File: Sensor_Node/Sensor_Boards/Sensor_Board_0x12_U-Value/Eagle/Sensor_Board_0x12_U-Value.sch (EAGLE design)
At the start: 28 parts, among them IC1 MCP3911A0-E/SS, IC2 4066D, J2 ARDUINO_ISP, J4 1x3 RA Female .1", J5 1x3 RA Female .1", U2 ATMEGA328P_TQFP, Y1 8MHZ

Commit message: Renamed U-value sensor board files
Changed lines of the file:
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@@
 <part name="U$1" library="wsn" deviceset="M04_SMD_90" device=""/>
 <part name="P+6" library="supply1" deviceset="VCC" device=""/>
-<part name="P+7" library="supply1" deviceset="VCC" device=""/>
 <part name="J4" library="wsn" deviceset="M03" device="SMD_RA_FEMALE" value="1x3 RA Female .1&quot;"/>
 <part name="J5" library="wsn" deviceset="M03" device="SMD_RA_FEMALE" value="1x3 RA Female .1&quot;"/>
@@
 <part name="GND17" library="supply1" deviceset="GND" device="" value="DGND"/>
 <part name="GND18" library="supply1" deviceset="GND" device="" value="DGND"/>
-<part name="GND19" library="supply1" deviceset="GND" device="" value="DGND"/>
 <part name="GND20" library="supply1" deviceset="GND" device="" value="DGND"/>
 <part name="GND21" library="supply1" deviceset="GND" device="" value="DGND"/>
@@
 <instance part="U$1" gate="G$1" x="29.21" y="81.788" rot="MR180"/>
 <instance part="P+6" gate="VCC" x="45.01" y="88.42"/>
-<instance part="P+7" gate="VCC" x="142.748" y="85.852"/>
 <instance part="J4" gate="J$1" x="155.194" y="72.898"/>
 <instance part="J5" gate="J$1" x="199.39" y="71.882"/>
@@
 <instance part="GND18" gate="1" x="175.006" y="65.016" smashed="yes">
 <attribute name="VALUE" x="173.736" y="67.556" size="1.778" layer="96" rot="R180"/>
-</instance>
-<instance part="GND19" gate="1" x="128.778" y="67.056" smashed="yes">
-<attribute name="VALUE" x="127.508" y="69.596" size="1.778" layer="96" rot="R180"/>
 </instance>
 <instance part="GND20" gate="1" x="99.568" y="75.692" smashed="yes">
@@
 </segment>
 <segment>
-<wire x1="126.492" y1="78.232" x2="142.748" y2="78.232" width="0.1524" layer="91"/>
-<pinref part="P+7" gate="VCC" pin="VCC"/>
-<wire x1="142.748" y1="78.232" x2="142.748" y2="83.312" width="0.1524" layer="91"/>
-</segment>
-<segment>
 <pinref part="P+6" gate="VCC" pin="VCC"/>
 <pinref part="U$1" gate="G$1" pin="1"/>
@@
 <label x="84.582" y="77.978" size="1.27" layer="95" xref="yes"/>
 </segment>
-<segment>
-<wire x1="126.29" y1="85.88" x2="127.508" y2="85.852" width="0.1524" layer="91"/>
-<label x="127.508" y="85.852" size="1.27" layer="95" xref="yes"/>
-</segment>
 </net>
 <net name="N$3" class="0">
@@
 <net name="FTDI_RXI" class="0">
 <segment>
-<wire x1="126.29" y1="83.34" x2="127.508" y2="83.312" width="0.1524" layer="91"/>
-<label x="127.508" y="83.312" size="1.27" layer="95" xref="yes"/>
-</segment>
-<segment>
 <pinref part="U2" gate="U$1" pin="PD1(TXD)"/>
 <wire x1="246.84" y1="150.65" x2="244.3" y2="150.65" width="0.1524" layer="91"/>
@@
 </net>
 <net name="FTDI_TXO" class="0">
-<segment>
-<wire x1="126.29" y1="80.8" x2="127.508" y2="80.772" width="0.1524" layer="91"/>
-<label x="127.508" y="80.772" size="1.27" layer="95" xref="yes"/>
-</segment>
 <segment>
 <pinref part="U2" gate="U$1" pin="PD0(RXD)"/>
@@
 </segment>
 <segment>
-<wire x1="126.29" y1="73.18" x2="128.778" y2="73.152" width="0.1524" layer="91"/>
-<wire x1="128.778" y1="73.152" x2="128.778" y2="69.596" width="0.1524" layer="91"/>
-<wire x1="126.29" y1="75.72" x2="128.778" y2="75.692" width="0.1524" layer="91"/>
-<wire x1="128.778" y1="75.692" x2="128.778" y2="73.152" width="0.1524" layer="91"/>
-<junction x="128.778" y="73.152"/>
-<pinref part="GND19" gate="1" pin="GND"/>
-</segment>
-<segment>

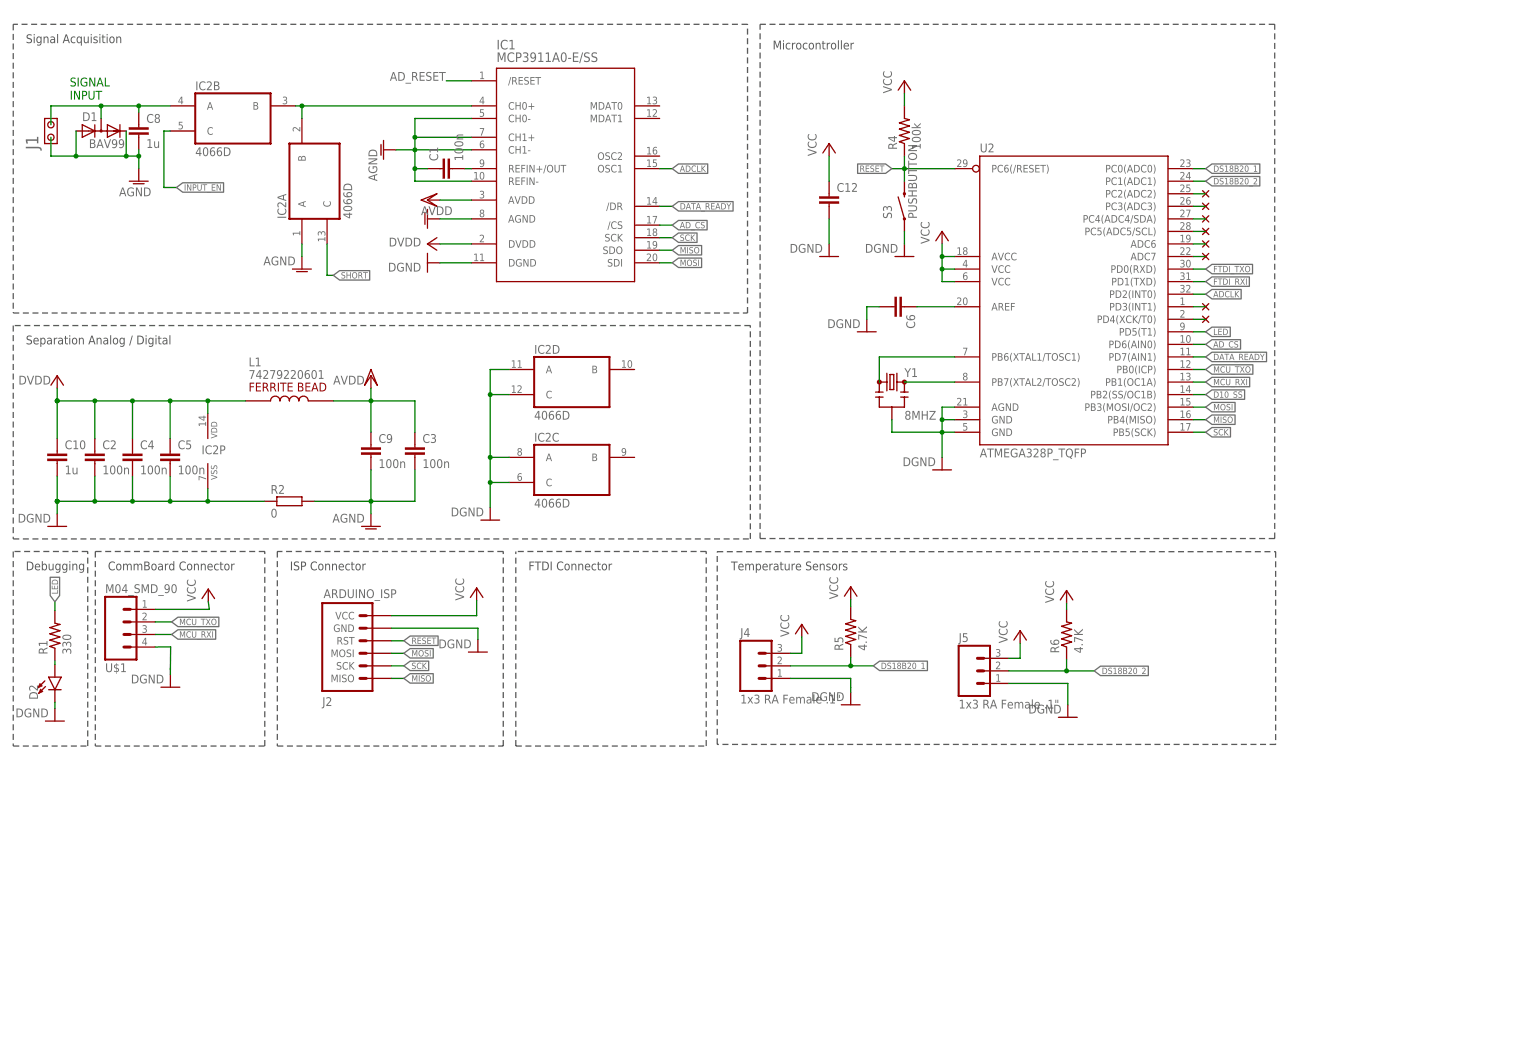
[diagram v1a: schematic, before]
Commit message: Renamed Heat_Flux to U-Value
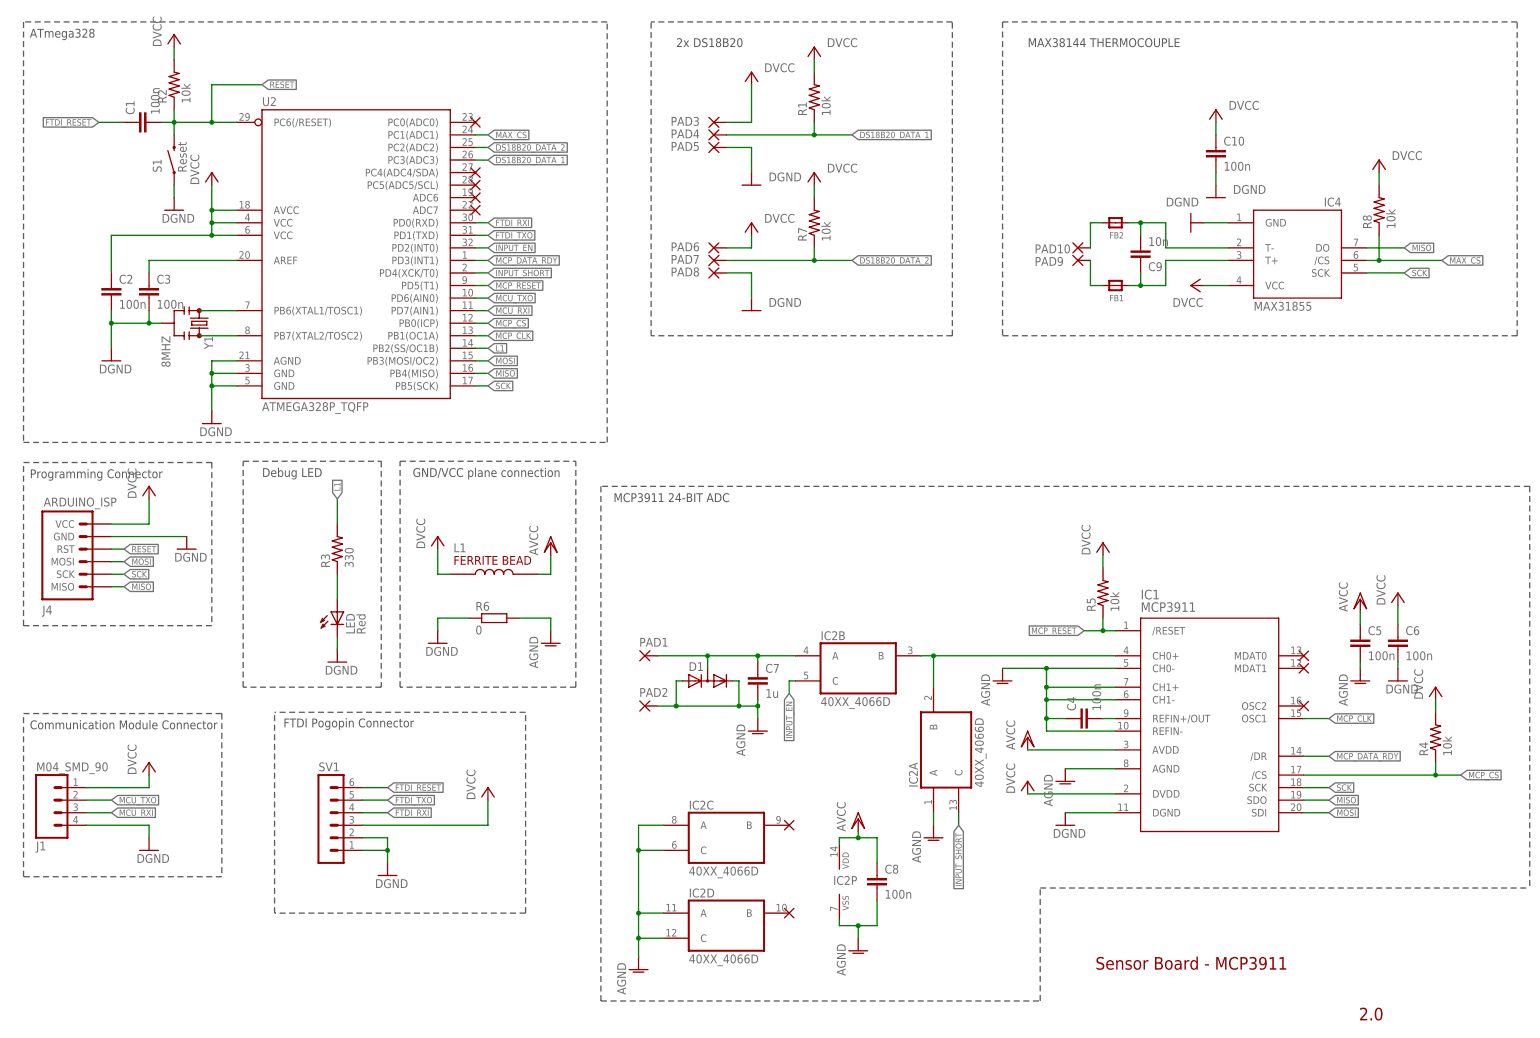
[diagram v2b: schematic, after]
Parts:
- removed C12: (no value), wsn:CAP0805
- removed D2: (no value), wsn:LED0603
- removed J2: ARDUINO_ISP, wsn:ARDUINO_ISP
- removed J5: 1x3 RA Female .1", wsn:M03SMD_RA_FEMALE
- removed S3: PUSHBUTTON, wsn:PUSHBUTTON
- removed U$1: M04_SMD_90, wsn:M04_SMD_90
- added C7: 1u, eagle-ltspice:C
- added FB1, FB2: (no value), Adafruit_MAX31855 v2:MICROBUILDER_FERRITE_0805MP
- added IC4: MAX31855, Adafruit_MAX31855 v2:ADAFRUIT_MAX31855
- added LED: Red, led:LEDSML0805
- added PAD1, PAD10, PAD2, PAD3, PAD4, PAD5, PAD6, PAD7, PAD8, PAD9: WIREPADSMD1,27-254, wirepad:WIREPADSMD1,27-254
- added R3: 330, SparkFun-Passives:RESISTOR0805-RES
- added R7, R8: 10k, SparkFun-Passives:RESISTOR0805-RES
- added S1: Reset, marc_library:PUSHBUTTON
- added SV1: (no value), con-lstb:MA06-1
- C1, C2, C3, C4, C5: device heatflow:C-EUC0805 -> eagle-ltspice:C
- C10, C8: value 1u -> 100n; device heatflow:C-EUC0805 -> eagle-ltspice:C
- C6: value (none) -> 100n; device wsn:CAP0805 -> eagle-ltspice:C
- C9: value 100n -> 10n; device heatflow:C-EUC0805 -> eagle-ltspice:C
- D1: value BAV99 -> LEDXLAMP_BAV99; device LEDXLamp:BAV99 -> Sensor_Board_0x07_Heat_Flux:LEDXLAMP_BAV99
- IC1: value MCP3911A0-E/SS -> MCP3911; device heatflow:MCP3911A0-E/SS -> Sensor_Board_0x07_Heat_Flux:HEATFLOW_MCP3911A0-E/SS
- IC2: value 4066D -> 40XX_4066D; device 40xx:4066D -> Sensor_Board_0x07_Heat_Flux:40XX_4066D
- J1: value (none) -> M04_SMD_90; device Stecker_Pins:CON2X1 -> myownthings:M04_SMD_90
- J4: value 1x3 RA Female .1" -> ARDUINO_ISP; device wsn:M03SMD_RA_FEMALE -> marc_library:ARDUINO_ISP
- L1: value 74279220601 -> HEATFLOW2_74279220601; device heatflow2:74279220601 -> Sensor_Board_0x07_Heat_Flux:HEATFLOW2_74279220601
- R1: value 330 -> 10k; device wsn:RESISTOR0805-RES -> SparkFun-Passives:RESISTOR0805-RES
- R2: value 0 -> 10k; device resistor:R-EU_M0805 -> SparkFun-Passives:RESISTOR0805-RES
- R4: value 100k -> 10k; device wsn:RESISTOR0805-RES -> SparkFun-Passives:RESISTOR0805-RES
- R5: value 4.7K -> 10k; device wsn:RESISTOR0805-RES -> SparkFun-Passives:RESISTOR0805-RES
- R6: value 4.7K -> 0; device wsn:RESISTOR0805-RES -> Sensor_Board_0x07_Heat_Flux:RESISTOR_R-EU_M0805
- U2: device wsn:ATMEGA328P_TQFP -> marc_library:ATMEGA328P_TQFP
- Y1: device wsn:RESONATOR8MHZ -> marc_library:RESONATOR8MHZ
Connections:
- removed net ADCLK: IC1.OSC1, U2.PD2(INT0)
- removed net AD_CS: IC1./CS, U2.PD6(AIN0)
- removed net AD_RESET: IC1./RESET
- removed net AVDD: C3.1, C9.1, IC1.AVDD, L1.P$2
- removed net D10_SS: U2.PB2(SS/OC1B)
- removed net DATA_READY: IC1./DR, U2.PD7(AIN1)
- removed net DS18B20_1: J4.2, R5.1, U2.PC0(ADC0)
- removed net DS18B20_2: J5.2, R6.1, U2.PC1(ADC1)
- removed net DVDD: C10.1, C2.1, C4.1, C5.1, IC1.DVDD, IC2P.VDD, L1.P$1
- removed net GND: C12.2, C6.2, D2.C, J2.GND, J5.1, S3.LEFT, U2.AGND, U2.GND@3, U2.GND@5, Y1.2
- removed net LED: R1.2, U2.PD5(T1)
- removed net N$10: U2.PC5(ADC5/SCL)
- removed net N$11: U2.ADC6
- removed net N$12: C8.1, D1.AC, IC2B.A, J1.2
- removed net N$13: U2.ADC7
- removed net N$17: U2.PD3(INT1)
- removed net N$18: U2.PD4(XCK/T0)
- removed net N$2 (its old number): C1.2, IC1.REFIN+/OUT
- removed net N$24: D2.A, R1.1
- removed net SHORT: IC2A.C
- removed net VCC: C12.1, J2.VCC, J4.3, J5.3, R4.2, R5.2, R6.2, U$1.1, U2.AVCC, U2.VCC@4, U2.VCC@6
- new net AVCC: C5.1, C8.1, IC1.AVDD, IC2P.VDD, L1.P$2
- new net DS18B20_DATA_1: PAD4.P, R1.1, U2.PC3(ADC3)
- new net DS18B20_DATA_2: PAD7.P, R7.1, U2.PC2(ADC2)
- new net DVCC: C10.1, C2.1, C6.1, IC1.DVDD, IC4.VCC, J1.1, J4.VCC, L1.P$1, PAD3.P, PAD6.P, R1.2, R2.2, R4.2, R5.2, R7.2, R8.2, SV1.3, U2.AVCC, U2.VCC@4, U2.VCC@6
- new net FTDI_RESET: C1.1, SV1.6
- new net INPUT_SHORT: IC2A.C, U2.PD4(XCK/T0)
- new net L1: R3.2, U2.PB2(SS/OC1B)
- new net MAX_CS: IC4./CS, R8.1, U2.PC1(ADC1)
- new net MCP_CLK: IC1.OSC1, U2.PB1(OC1A)
- new net MCP_CS: IC1./CS, R4.1, U2.PB0(ICP)
- new net MCP_DATA_RDY: IC1./DR, U2.PD3(INT1)
- new net MCP_RESET: IC1./RESET, R5.1, U2.PD5(T1)
- new net N$30: LED.A, R3.1
- new net N$8: C9.2, FB2.P$2, IC4.T-
- net AGND: now also C4.1, C5.2, C7.2, IC2C.A, IC2C.C, IC2D.A, IC2D.C, IC2P.VSS, PAD2.P, R6.2; no longer C1.1, C3.2, C9.2, J1.1, R2.2
- net DGND: now also C3.2, C6.2, IC4.GND, J1.4, J4.GND, LED.C, PAD5.P, PAD8.P, R6.1, S1.LEFT, SV1.1, SV1.2, U2.AGND, U2.GND@3, U2.GND@5, Y1.2; no longer C4.2, C5.2, IC2C.A, IC2C.C, IC2D.A, IC2D.C, IC2P.VSS, R2.1
- net FTDI_RXI: now also SV1.4, U2.PD0(RXD); no longer U2.PD1(TXD)
- net FTDI_TXO: now also SV1.5, U2.PD1(TXD); no longer U2.PD0(RXD)
- net INPUT_EN: now also U2.PD2(INT0)
- net MCU_RXI: now also J1.3, U2.PD7(AIN1); no longer U$1.3, U2.PB1(OC1A)
- net MCU_TXO: now also J1.2, U2.PD6(AIN0); no longer U$1.2, U2.PB0(ICP)
- net MISO: now also IC4.DO, J4.MISO; no longer J2.MISO
- net MOSI: now also J4.MOSI; no longer J2.MOSI
- net N$15: now also C3.1, U2.AREF; no longer J4.1
- net N$3: now also FB1.P$1, PAD9.P; no longer C6.1, U2.AREF
- net N$4: now also C4.2, IC1.REFIN+/OUT; no longer U$1.4
- net N$6: now also C7.1, D1.AC, IC2B.A, PAD1.P; no longer U2.PC2(ADC2)
- net N$7: now also FB2.P$1, PAD10.P; no longer U2.PC3(ADC3)
- net N$9: now also C9.1, FB1.P$2, IC4.T+; no longer U2.PC4(ADC4/SDA)
- net RESET: now also C1.2, J4.RST, R2.1, S1.RIGHT; no longer J2.RST, R4.1, S3.RIGHT
- net SCK: now also IC4.SCK, J4.SCK; no longer J2.SCK
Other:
- note added: "2.0"
- note added: "2x DS18B20"
- note added: "ATmega328"
- note added: "Communication Module Connector"
- note added: "Debug LED"
- note added: "FTDI Pogopin Connector"
- note added: "GND/VCC plane connection"
- note added: "MAX38144 THERMOCOUPLE"
- note added: "MCP3911 24-BIT ADC"
- note added: "Programming Connector"
- note added: "Sensor Board - MCP3911"
- note removed: "CommBoard Connector"
- note removed: "Debugging"
- note removed: "FTDI Connector"
- note removed: "ISP Connector"
- note removed: "Microcontroller"
- note removed: "SIGNAL INPUT"
- note removed: "Separation Analog / Digital"
- note removed: "Signal Acquisition"
- note removed: "Temperature Sensors"
- moved on the sheet: C1, C10, C2, C3, C4, C5, C6, C8, C9, IC1, IC2A, IC2B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
